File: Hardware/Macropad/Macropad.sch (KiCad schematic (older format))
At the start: 0 parts

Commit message: Schematic mostly done. Started grouping components in layout
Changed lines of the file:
@@
 $Descr A4 11693 8268
 encoding utf-8
-Sheet 1 5
+Sheet 1 6
 Title ""
 Date ""
@@
 F1 "uController.sch" 50
 $EndSheet
+$Sheet
+S 3750 5000 2250 1275
+U 6247A5CE
+F0 "USB_HUB" 50
+F1 "USB_HUB.sch" 50
+$EndSheet
 $EndSCHEMATC

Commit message: First pass of the layout done
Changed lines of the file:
@@
 S 1000 3000 2250 1275
 U 6114D32E
-F0 "USB" 50
+F0 "USB" 118
 F1 "USB.sch" 50
 $EndSheet
@@
 S 3750 3000 2250 1250
 U 61150193
-F0 "Switches" 50
+F0 "Switches" 118
 F1 "Switches.sch" 50
 $EndSheet
@@
 S 6500 3000 2250 1250
 U 61D5AB4C
-F0 "LEDs" 50
+F0 "LEDs" 118
 F1 "LEDs.sch" 50
 $EndSheet
@@
 S 1000 5000 2250 1250
 U 62022D96
-F0 "uController" 50
+F0 "uController" 118
 F1 "uController.sch" 50
 $EndSheet
@@
 S 3750 5000 2250 1275
 U 6247A5CE
-F0 "USB_HUB" 50
+F0 "USB_HUB" 118
 F1 "USB_HUB.sch" 50
 $EndSheet

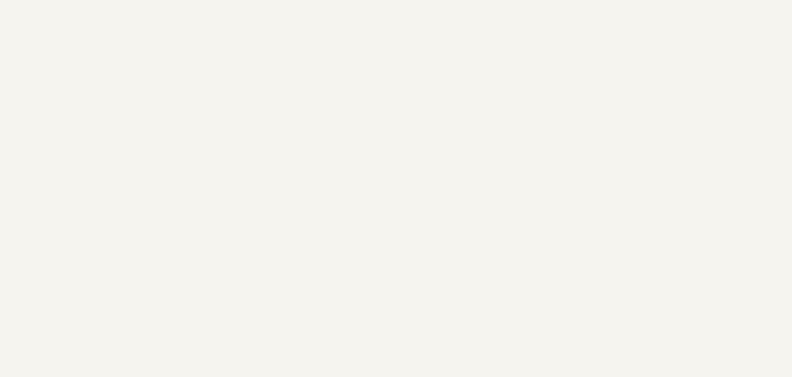
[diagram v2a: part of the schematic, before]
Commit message: Updating 3D models, mapping models for USB and encoder
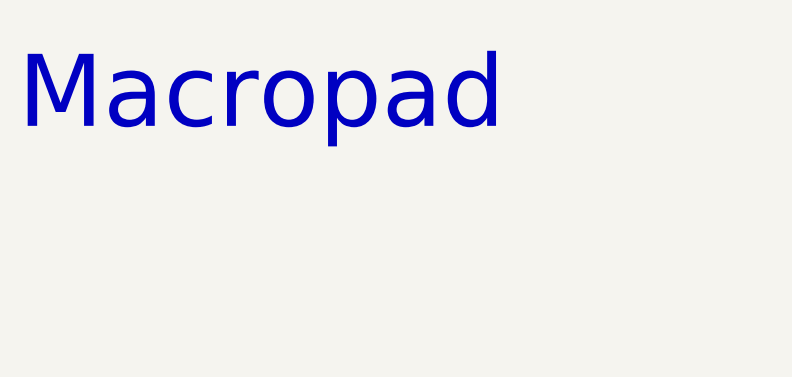
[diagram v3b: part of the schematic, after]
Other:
- note added: "Macropad"
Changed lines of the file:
@@
 F1 "USB_HUB.sch" 50
 $EndSheet
+Text Notes 750  1000 0    315  ~ 0
+Macropad
 $EndSCHEMATC
